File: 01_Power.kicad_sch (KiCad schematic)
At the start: 25 parts, among them Q1 SI3421DV, Q2 SI3421DV, U1 CYPD3177_24x

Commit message: settle on a layout
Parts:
- added J3: Screw_Terminal_01x02, CakeUSB:TerminalBlock_WJ103-5.0-2P, symbol Connector:Screw_Terminal_01x02
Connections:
- net +20V: now also J3.1 (Pin_1)
- net GND: now also J3.2 (Pin_2)
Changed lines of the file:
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@@
+    (stroke (width 0) (type default))
+  )
+  (wire (pts (xy 236.22 91.44) (xy 236.22 92.71))
     (stroke (width 0) (type default))
   )
@@
     (stroke (width 0) (type default))
   )
+  (wire (pts (xy 233.68 92.71) (xy 233.68 91.44))
+    (stroke (width 0) (type default))
+  )
   (wire (pts (xy 170.18 27.178) (xy 170.18 29.718))
     (stroke (width 0) (type default))
@@
     (stroke (width 0) (type default))
   )
+  (wire (pts (xy 231.14 95.25) (xy 231.14 92.71))
+    (stroke (width 0) (type default))
+  )
   (wire (pts (xy 147.447 29.972) (xy 152.527 29.972))
     (stroke (width 0) (type default))
@@
     (stroke (width 0) (type default))
   )
+  (wire (pts (xy 236.22 92.71) (xy 238.76 92.71))
+    (stroke (width 0) (type default))
+  )
   (wire (pts (xy 103.759 37.592) (xy 103.759 37.338))
     (stroke (width 0) (type default))
@@
     (stroke (width 0) (type default))
   )
+  (wire (pts (xy 238.76 92.71) (xy 238.76 95.25))
+    (stroke (width 0) (type default))
+  )
   (wire (pts (xy 173.99 67.31) (xy 173.99 68.58))
     (stroke (width 0) (type default))
@@
   )
   (wire (pts (xy 228.6 45.72) (xy 228.6 47.244))
+    (stroke (width 0) (type default))
+  )
+  (wire (pts (xy 231.14 92.71) (xy 233.68 92.71))
     (stroke (width 0) (type default))
   )
@@
     )
   )
+  (symbol (lib_id "Connector:Screw_Terminal_01x02") (at 233.68 86.36 90) (unit 1)
+    (in_bom yes) (on_board yes) (dnp no) (fields_autoplaced)
+    (property "Reference" "J3" (at 238.76 85.09 90)
+      (effects (font (size 1.27 1.27)) (justify right))
+    )
+    (property "Value" "Screw_Terminal_01x02" (at 238.76 87.63 90)
+      (effects (font (size 1.27 1.27)) (justify right))
+    )
+    (property "Footprint" "CakeUSB:TerminalBlock_WJ103-5.0-2P" (at 233.68 86.36 0)
+      (effects (font (size 1.27 1.27)) hide)
+    )
+    (property "Datasheet" "~" (at 233.68 86.36 0)
+      (effects (font (size 1.27 1.27)) hide)
+    )
+    (pin "2")
+    (pin "1")
+    (instances
+      (project "USBHUB"
+        (path "/d5edc647-9ac3-4ac1-ab8a-57c77be3f4d3/2bd96af5-5a66-4797-badd-32cacbbf4fbd"
+          (reference "J3") (unit 1)
+        )
+      )
+    )
+  )
   (symbol (lib_id "power:GND") (at 228.6 47.244 0) (unit 1)
     (in_bom yes) (on_board yes) (dnp no) (fields_autoplaced)
@@
     )
   )
+  (symbol (lib_id "power:GND") (at 238.76 95.25 0) (unit 1)
+    (in_bom yes) (on_board yes) (dnp no) (fields_autoplaced)
+    (property "Reference" "#PWR0108" (at 238.76 101.6 0)
+      (effects (font (size 1.27 1.27)) hide)
+    )
+    (property "Value" "GND" (at 238.76 100.33 0)
+      (effects (font (size 1.27 1.27)))
+    )
+    (property "Footprint" "" (at 238.76 95.25 0)
+      (effects (font (size 1.27 1.27)) hide)
+    )
+    (property "Datasheet" "" (at 238.76 95.25 0)
+      (effects (font (size 1.27 1.27)) hide)
+    )
+    (pin "1")
+    (instances
+      (project "USBHUB"
+        (path "/d5edc647-9ac3-4ac1-ab8a-57c77be3f4d3/2bd96af5-5a66-4797-badd-32cacbbf4fbd"
+          (reference "#PWR0108") (unit 1)
+        )
+      )
+    )
+  )
   (symbol (lib_id "power:GND") (at 134.747 116.332 0) (unit 1)
     (in_bom yes) (on_board yes) (dnp no) (fields_autoplaced)
@@
         )
       )
+    )
+  )
+  (symbol (lib_id "USBHUBSymbols:+20V") (at 231.14 95.25 180) (unit 1)
+    (in_bom yes) (on_board yes) (dnp no) (fields_autoplaced)
+    (property "Reference" "#PWR0106" (at 231.14 91.44 0)
+      (effects (font (size 1.27 1.27)) hide)
+    )
+    (property "Value" "+20V" (at 231.14 100.33 0)
+      (effects (font (size 1.27 1.27)))
+    )
+    (property "Footprint" "" (at 231.14 95.25 0)
+      (effects (font (size 1.27 1.27)) hide)
+    )
+    (property "Datasheet" "" (at 231.14 95.25 0)
+      (effects (font (size 1.27 1.27)) hide)
+    )
+    (pin "1")
+    (instances
+      (project "USBHUB"
+        (path "/d5edc647-9ac3-4ac1-ab8a-57c77be3f4d3/2bd96af5-5a66-4797-badd-32cacbbf4fbd"
+          (reference "#PWR0106") (unit 1)
+        )
+      )

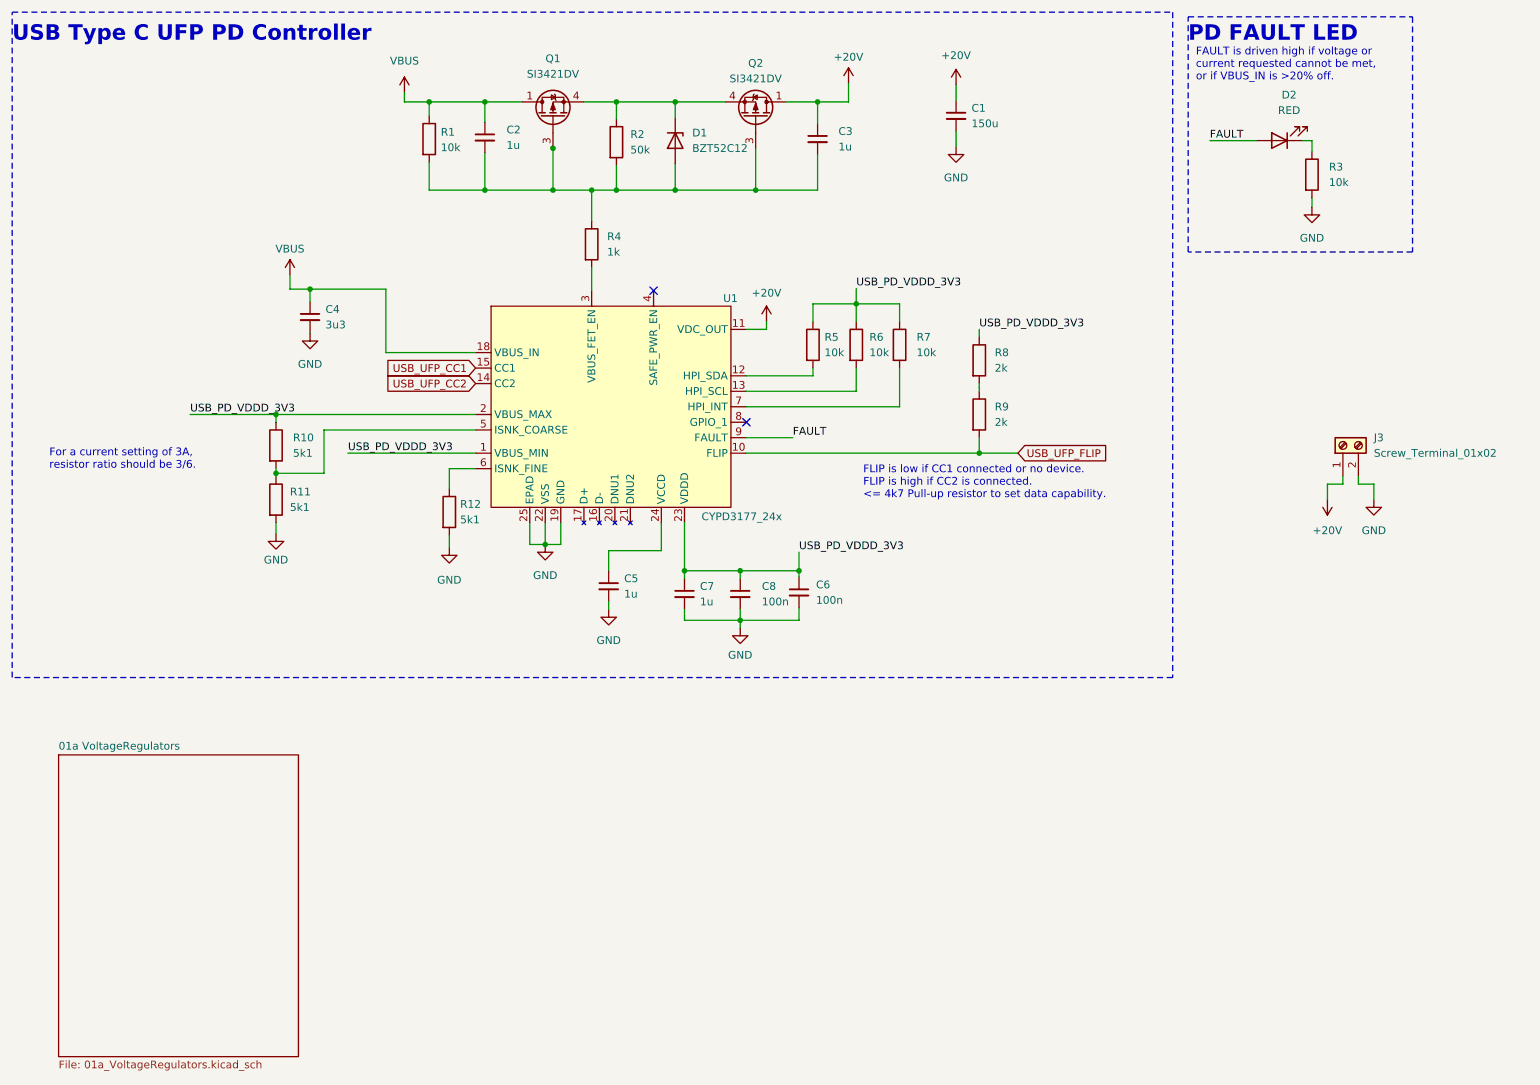
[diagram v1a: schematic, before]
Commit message: add schottky for usb pd
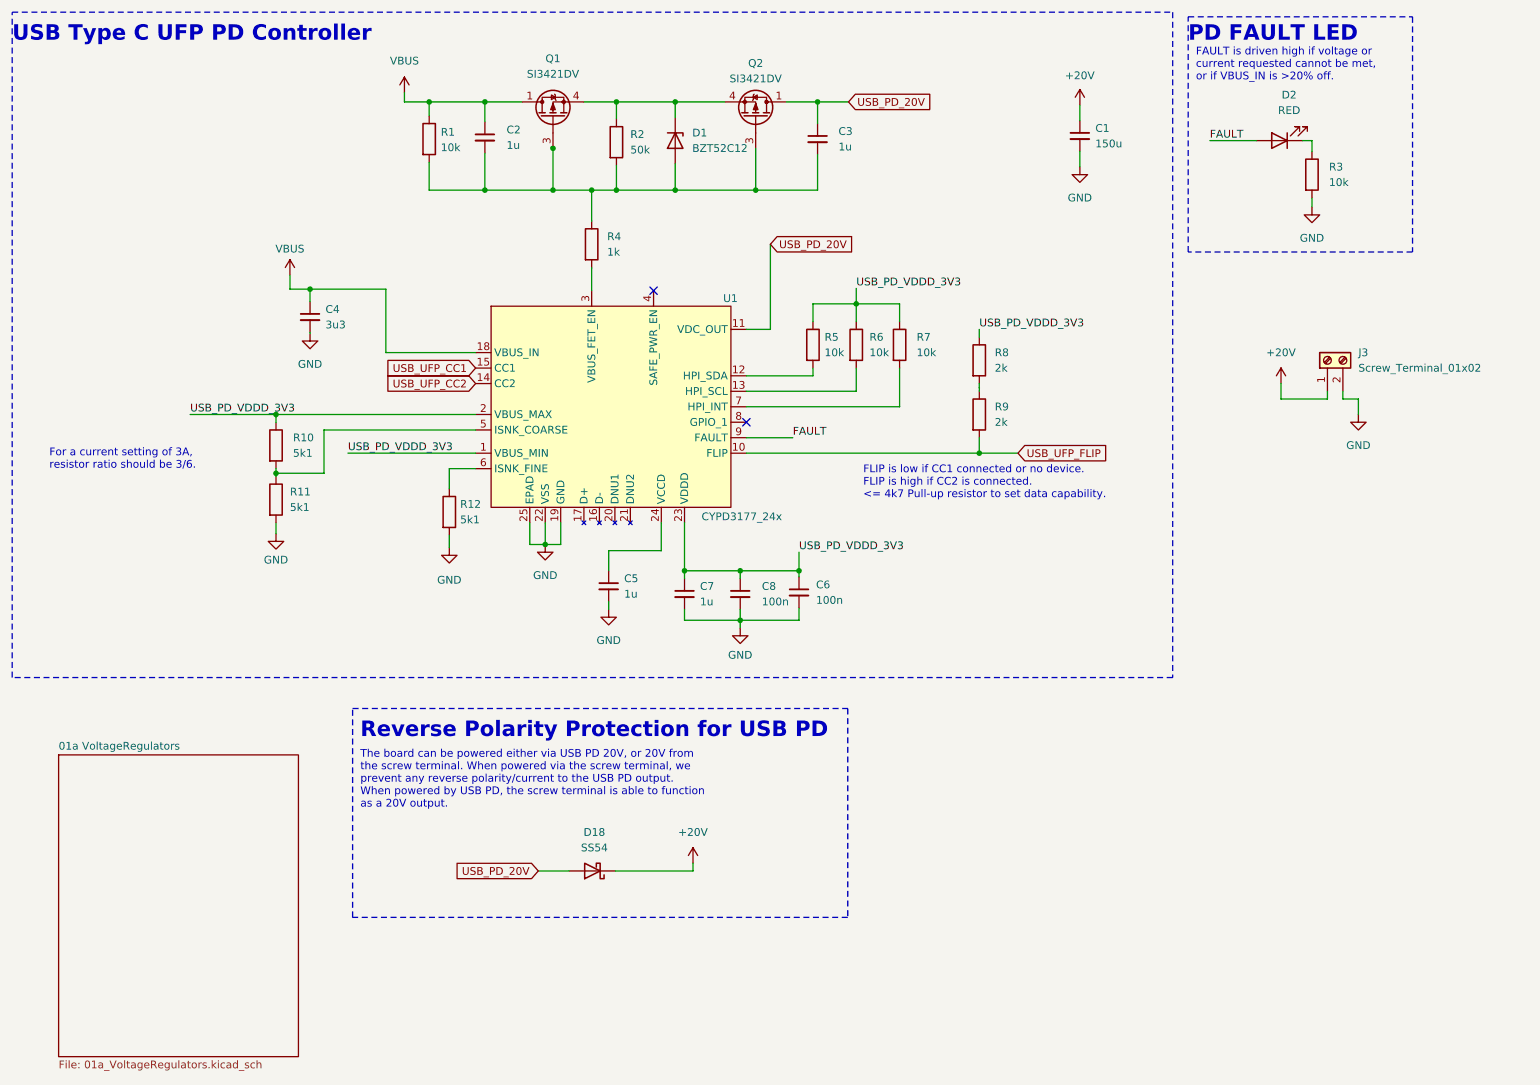
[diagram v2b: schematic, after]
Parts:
- added D18: SS54, Diode_SMD:D_SMA, symbol Device:D_Schottky
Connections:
- net +20V: now also D18.1 (K); no longer C3.1, Q2.1 (D), Q2.2 (D1), Q2.5 (D2), Q2.6 (D3), U1.11 (VDC_OUT)
- new net USB_PD_20V: C3.1, D18.2 (A), Q2.1 (D), Q2.2 (D1), Q2.5 (D2), Q2.6 (D3), U1.11 (VDC_OUT)
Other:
- note added: "Reverse Polarity Protection for USB PD"
- note added: "The board can be powered either via USB PD 20V, or 20V from the screw terminal. When powered via the screw terminal, we prevent any reverse polarity/current to the USB PD output. When powered by USB PD, the screw terminal is able to function as a 20V output."
- moved on the sheet: C1
